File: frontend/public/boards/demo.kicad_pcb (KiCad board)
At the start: 2 copper layers, 70 x 50 mm, 3 parts, among them U1 ATmega328P

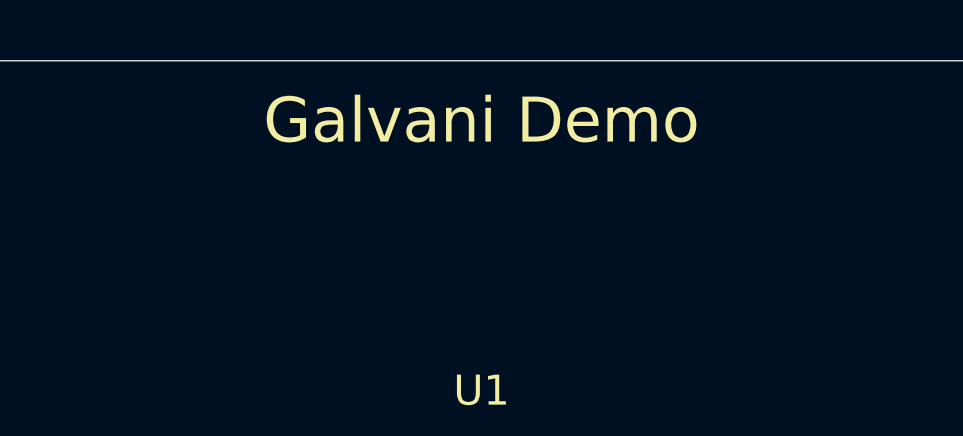
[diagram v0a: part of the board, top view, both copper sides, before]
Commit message: Rename product hauksbee to hauksbee
Mechanical rename of the brand across the workspace:
- 8 crates hauksbee-* -> hauksbee-* (dirs via git mv, package/lib/path-dep names)
- binaries: hauksbee -> hauksbee, hauksbee-ci -> hauksbee-ci
- crate idents hauksbee_* -> hauksbee_*, HauksbeeEngine -> HauksbeeEngine
- all HAUKSBEE_* env vars -> HAUKSBEE_* (corpus, qemu, renode, extract-mock, etc)
- install/config dirs: ~/.hauksbee -> ~/.hauksbee, ~/.config/hauksbee -> ~/.config/hauksbee,
 ~/.hauksbee-qemu-esp -> ~/.hauksbee-qemu-esp
- docs, integrations (github-action, kicad-plugin, pre-commit), scripts, frontend branding
- repo refs ETM-Code/hauksbee -> ETM-Code/hauksbee, domain hauksbee.dev
- kicad-forge crates (forge-*) deliberately NOT renamed; forge path-deps preserved
- NAMING.md keeps its historical content, gains a decision note
- boot-coverage qemu_xtensa_available() now reuses the backend is_available
 (real -machine help esp32 check) so ESP32 co-sim tests skip cleanly on stock qemu
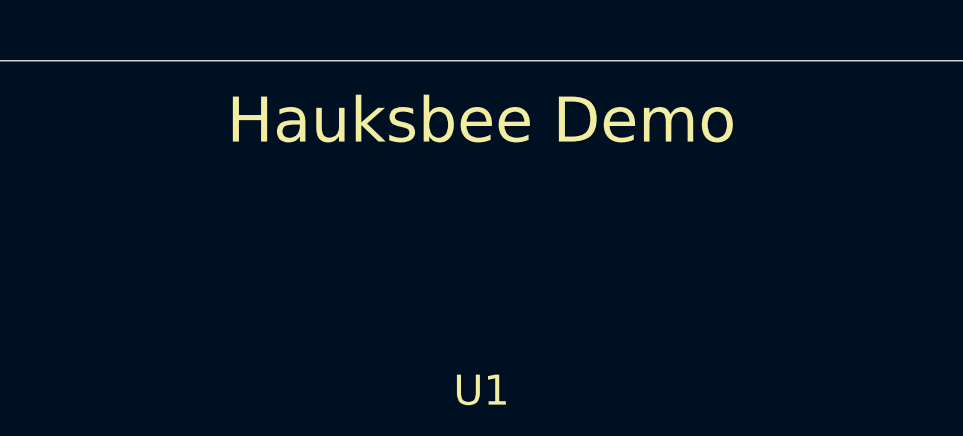
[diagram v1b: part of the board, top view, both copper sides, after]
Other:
- board text added: "Hauksbee Demo"
- board text removed: "Galvani Demo"
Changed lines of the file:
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@@
 (kicad_pcb
 	(version 20260206)
-	(generator "galvani-demo")
+	(generator "hauksbee-demo")
 	(general
 		(thickness 1.6)
@@
 	(paper "A4")
 	(title_block
-		(title "Galvani Demo Board")
+		(title "Hauksbee Demo Board")
 	)
 	(layers
@@
 		(width 0.05)
 	)
-	(gr_text "Galvani Demo"
+	(gr_text "Hauksbee Demo"
 		(at 35 2)
 		(layer "F.SilkS")
